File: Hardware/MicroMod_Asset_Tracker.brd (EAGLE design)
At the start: 76.2 x 76.2 mm, 338 parts, among them IC1 SN74AVC4T774PW, IC2 SN74AVC4T774PW, IC3 SN74AVC4T774PW, J11 microSD, J13 TP, J17 NANO_SIM, J18 SARA_USB, J19 NI, J2 JTAG, J4 MICROMOD-2222-C, J5 SPI, J6 DIAG, J7 QWIIC_RIGHT_ANGLE, J9 !RST!, Q1 310mA/60V/1.6Ω, Q10 20V/0.2A/8MHz/1.2Ω/1Vth, Q2 310mA/60V/1.6Ω, Q3 310mA/60V/1.6Ω, Q4 310mA/60V/1.6Ω, Q5 20V/0.2A/8MHz/1.2Ω/1Vth, Q6 20V/4.2A/52mΩ/1.4W, Q7 310mA/60V/1.6Ω, U1 SARA-R5, U13 9DoF IMU, U14 1.8V/100mA, U2 MCP73831, U3 3.3V, U5 AP7361C-33FGE, U7 PCA9306, U8 74HC1G04

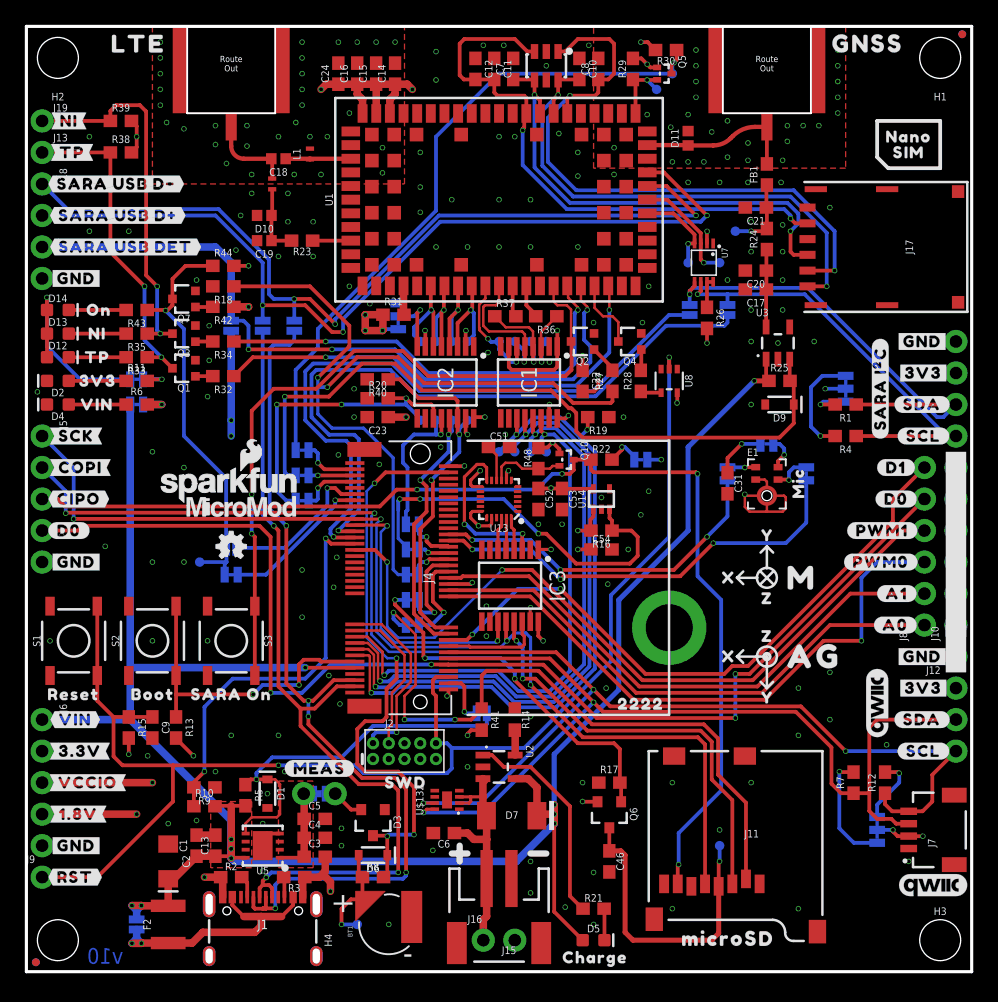
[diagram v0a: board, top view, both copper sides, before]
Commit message: Added the missing PROD_IDs
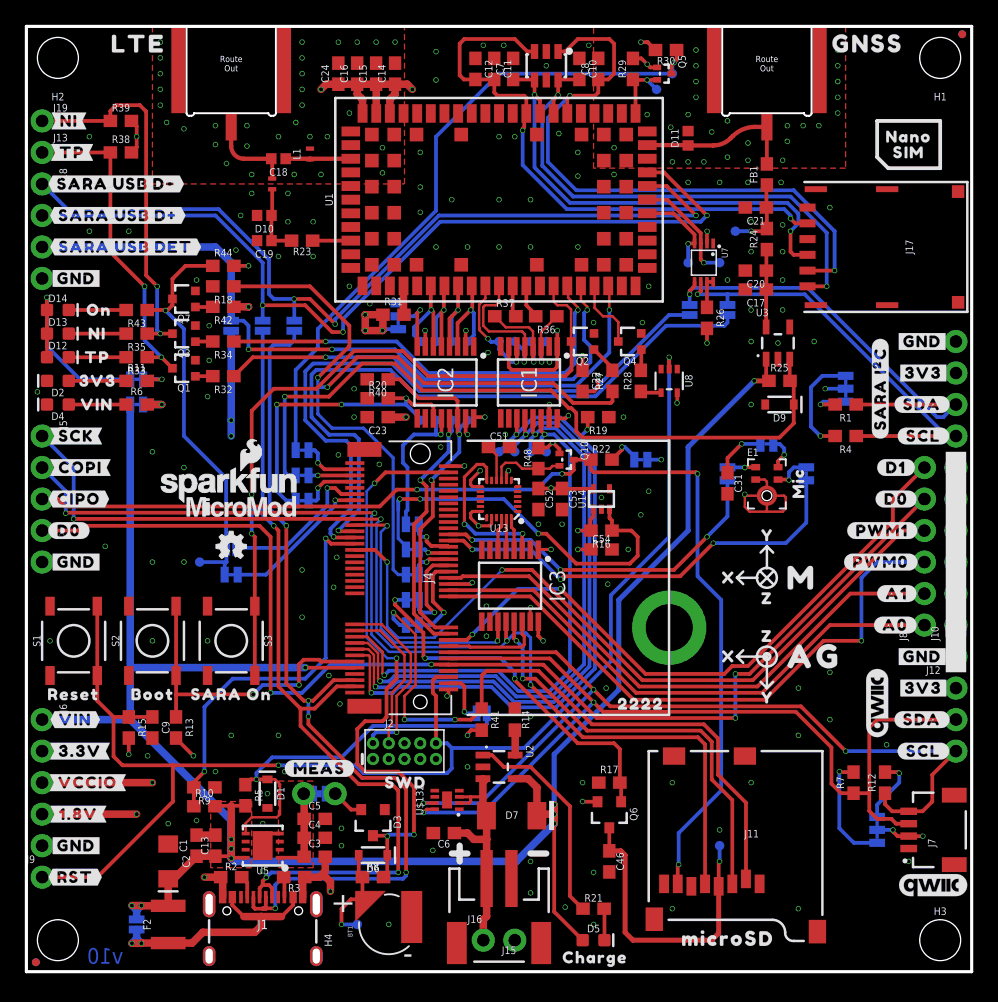
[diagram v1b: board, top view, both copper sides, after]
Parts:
- E3, E4: device New_Parts:SMA-EDGE-SMD -> SparkFun-RF:SMA-EDGE-SMD
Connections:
- net GND: now also U$132.1, U$132.4, U$132.6, U$132.9; no longer U$132.P$1, U$132.P$4, U$132.P$6, U$132.P$9
- net I2C_SCL: now also U$132.7; no longer U$132.P$7
- net I2C_SDA: now also U$132.8; no longer U$132.P$8
- net V_BATT: now also U$132.2, U$132.3; no longer U$132.P$2, U$132.P$3
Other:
- board text added: "HASL Finish"
- board text removed: "ENIG Finish"

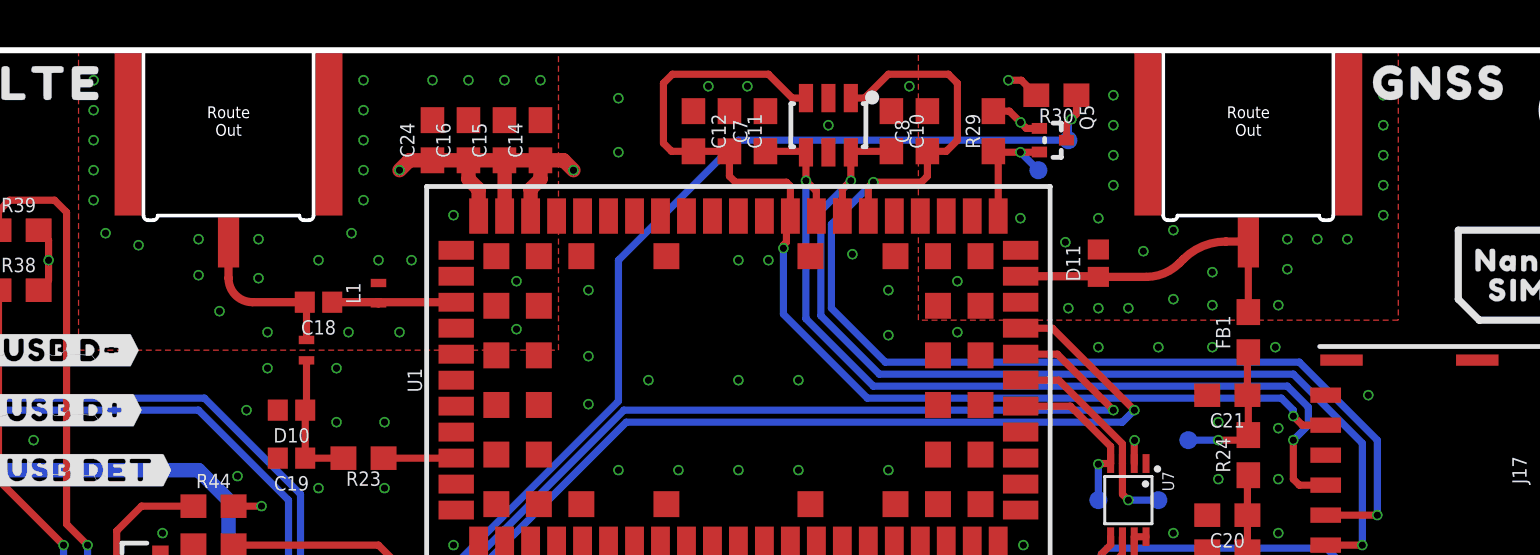
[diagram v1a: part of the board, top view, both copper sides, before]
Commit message: Updated to use the revised SMD SMA connector footprint
The footprint for the SMA now includes the toolpath for a 1mm end-mill
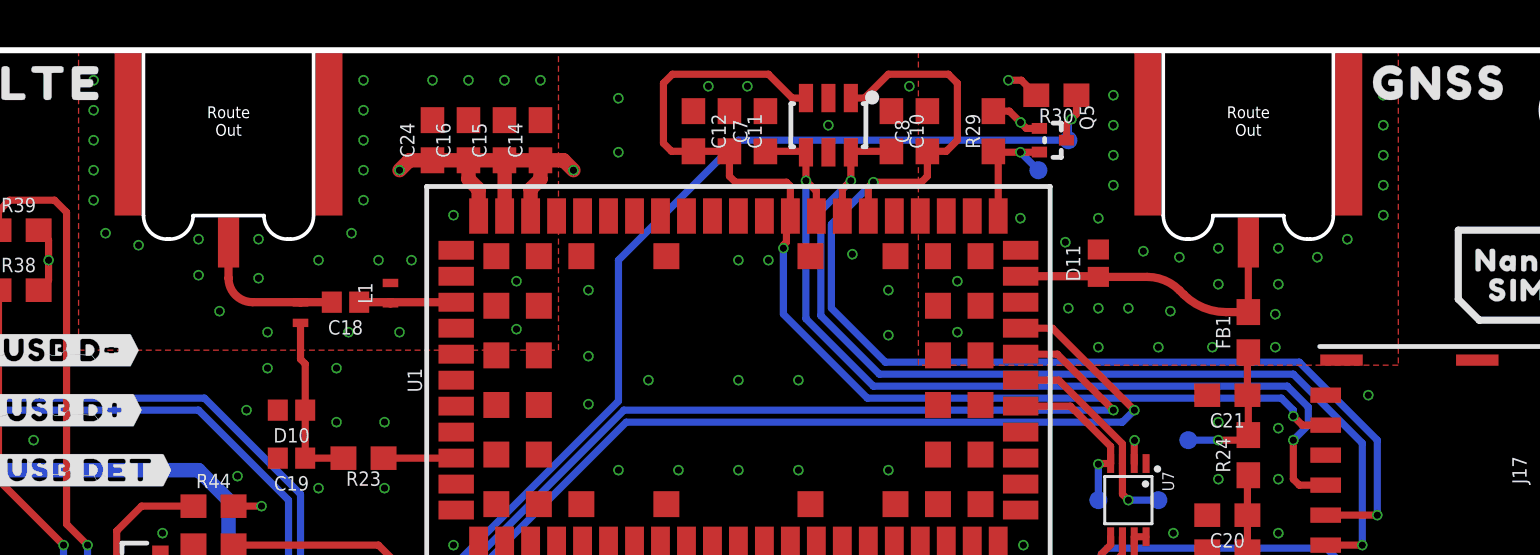
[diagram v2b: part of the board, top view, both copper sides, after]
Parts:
- moved L2 1.61 mm to (19.6, 65.1)
- moved C18 1.14 mm to (21.5, 65.5)
- moved L1 0.51 mm to (23.4, 65.9)
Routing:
- net N$16: track 5.78 -> 7.71 mm
- net SARA_ANT: track 5.29 -> 4.15 mm

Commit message: Updates for V11 of the PCB
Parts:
- removed R13: 100k, SparkFun-Resistors:0603
- added U$133: (no value), output:#VIN#3#0
- added VIN/3: JUMPER-SMT_2_NC_TRACE_SILK, SparkFun-Jumpers:SMT-JUMPER_2_NC_TRACE_SILK
- R33: value 470 -> 100
- moved U$28 1.05 mm to (50.9, 2.70)
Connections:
- new net N$18: R10.2, VIN/3.1
- net !BOOT!: no longer R13.1
- net 3.3V: no longer R13.2
- net VIN: now also VIN/3.2; no longer R10.2
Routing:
- net N$18: track 0.00 -> 4.38 mm, vias 0 -> 1
- net !BOOT!: track 25.5 -> 23.5 mm
- net 3.3V: track 69.1 -> 67.1 mm, vias 24 -> 23
- net GND: vias 191 -> 192
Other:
- board text added: "v11"
- board text removed: "v10"
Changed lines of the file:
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@@
 <?xml version="1.0" encoding="utf-8"?>
 <!DOCTYPE eagle SYSTEM "eagle.dtd">
-<eagle version="9.6.0">
+<eagle version="9.6.2">
 <drawing>
 <settings>
@@
 <wire x1="76.2" y1="0" x2="0" y2="0" width="0.254" layer="20"/>
 <rectangle x1="74.1045" y1="26.9875" x2="75.7555" y2="41.91" layer="21"/>
-<text x="6.35" y="1.27" size="1.27" layer="16" font="vector" ratio="20" rot="MR0" align="center">v10</text>
+<text x="6.35" y="1.27" size="1.27" layer="16" font="vector" ratio="20" rot="MR0" align="center">v11</text>
 <wire x1="35.56" y1="42.799" x2="51.805" y2="42.799" width="0.2032" layer="21"/>
 <wire x1="51.805" y1="42.799" x2="51.805" y2="20.701" width="0.2032" layer="21"/>
@@
 <element name="U$4" library="output" package="#3V3#0" value="" x="8.001" y="47.752" smashed="yes" rot="MR0"/>
 <element name="U$20" library="output" package="#VIN#1" value="" x="8.001" y="45.72" smashed="yes" rot="MR0"/>
-<element name="U$28" library="output" package="MICROSD0" value="" x="51.943" y="2.667" smashed="yes"/>
+<element name="U$28" library="output" package="MICROSD0" value="" x="50.89525" y="2.69875" smashed="yes"/>
 <element name="LOGO5" library="SparkFun-Aesthetics" package="ORDERING_INSTRUCTIONS" value="SPECIAL_INSTRUCTIONS-ORDERING" x="80.01" y="50.8" smashed="yes"/>
 <element name="J7" library="SparkFun-Connectors" package="JST04_1MM_RA" value="QWIIC_RIGHT_ANGLE" x="71.12" y="11.43" smashed="yes" rot="R90">
@@
 <attribute name="VALUE" x="9.398" y="19.685" size="0.6096" layer="27" font="vector" ratio="20" rot="R270" align="top-center"/>
 </element>
-<element name="R13" library="SparkFun-Resistors" package="0603" value="100k" x="12.065" y="19.685" smashed="yes" rot="R270">
-<attribute name="NAME" x="12.827" y="19.685" size="0.6096" layer="25" font="vector" ratio="20" rot="R270" align="bottom-center"/>
-<attribute name="PROD_ID" value="RES-07828" x="12.065" y="19.685" size="1.778" layer="27" ratio="15" rot="R270" display="off"/>
-<attribute name="VALUE" x="11.303" y="19.685" size="0.6096" layer="27" font="vector" ratio="20" rot="R270" align="top-center"/>
-</element>
 <element name="U1" library="SARA_R5" package="SARA-LGA" value="SARA-R5" x="38.1" y="62.23" smashed="yes">
 <attribute name="NAME" x="24.7" y="62.23" size="0.6096" layer="25" font="vector" ratio="20" rot="R90" align="bottom-center"/>
@@
 <attribute name="VALUE" x="15.875" y="48.768" size="0.6096" layer="27" font="vector" ratio="20" rot="R180" align="top-center"/>
 </element>
-<element name="R33" library="SparkFun-Resistors" package="0603" value="470" x="8.89" y="49.53" smashed="yes" rot="R180">
+<element name="R33" library="SparkFun-Resistors" package="0603" value="100" x="8.89" y="49.53" smashed="yes" rot="R180">
 <attribute name="NAME" x="8.89" y="48.768" size="0.6096" layer="25" font="vector" ratio="20" rot="R180" align="bottom-center"/>
-<attribute name="PROD_ID" value="RES-07869" x="8.89" y="49.53" size="1.778" layer="27" ratio="15" rot="R180" display="off"/>
-<attribute name="VALUE" value="470" x="8.89" y="50.292" size="0.6096" layer="27" font="vector" ratio="20" rot="R180" align="top-center"/>
+<attribute name="PROD_ID" value="RES-07863" x="8.89" y="49.53" size="1.778" layer="27" ratio="15" rot="R180" display="off"/>
+<attribute name="VALUE" value="100" x="8.89" y="50.292" size="0.6096" layer="27" font="vector" ratio="20" rot="R180" align="top-center"/>
 </element>
 <element name="D12" library="SparkFun-LED" package="LED-0603" value="GREEN" x="2.54" y="49.53" smashed="yes">
@@
 <attribute name="VALUE" x="36.449" y="13.843" size="0.6096" layer="27" font="vector" ratio="20" rot="R90" align="bottom-center"/>
 </element>
+<element name="VIN/3" library="SparkFun-Jumpers" package="SMT-JUMPER_2_NC_TRACE_SILK" package3d_urn="urn:adsk.eagle:package:39281/1" value="JUMPER-SMT_2_NC_TRACE_SILK" x="16.47825" y="14.63675" smashed="yes" rot="MR270">
+<attribute name="NAME" x="15.33525" y="14.63675" size="0.6096" layer="26" font="vector" ratio="20" rot="MR270" align="bottom-center"/>
+</element>
+<element name="U$133" library="output" package="#VIN#3#0" value="" x="14.478" y="14.70025" smashed="yes" rot="MR270"/>
 </elements>
 <signals>
@@
 <contactref element="U$132" pad="6"/>
 <via x="46.736" y="22.86" extent="1-16" drill="0.3"/>
+<via x="17.653" y="16.0655" extent="1-16" drill="0.3"/>
 </signal>
 <signal name="3.3V">
@@
 <contactref element="J12" pad="2"/>
 <contactref element="R15" pad="2"/>
-<contactref element="R13" pad="2"/>
 <contactref element="C54" pad="1"/>
 <contactref element="U14" pad="1"/>
@@
 <wire x1="50.077" y1="74.93" x2="49.53" y2="74.93" width="0.3048" layer="1"/>
 <via x="8.255" y="17.526" extent="1-16" drill="0.3"/>
-<via x="13.462" y="17.399" extent="1-16" drill="0.3"/>
 <wire x1="8.255" y1="18.835" x2="8.255" y2="17.526" width="0.3048" layer="1"/>
-<wire x1="12.065" y1="18.835" x2="12.065" y2="18.796" width="0.3048" layer="1"/>
-<wire x1="12.065" y1="18.796" x2="13.462" y2="17.399" width="0.3048" layer="1"/>
 <via x="35.306" y="40.767" extent="1-16" drill="0.3"/>
 <wire x1="34.025" y1="40.75" x2="35.289" y2="40.75" width="0.3048" layer="1"/>
@@
 <contactref element="BYP" pad="2"/>
 <contactref element="F2" pad="2"/>
-<contactref element="R10" pad="2"/>
 <contactref element="C1" pad="1"/>
 <contactref element="R5" pad="2"/>
@@
 <wire x1="13.716" y1="9.31" x2="15.24" y2="9.31" width="0.6096" layer="1"/>
 <wire x1="15.365" y1="9.185" x2="15.24" y2="9.31" width="0.3048" layer="1"/>
-<wire x1="15.201" y1="13.335" x2="15.24" y2="13.374" width="0.3048" layer="1"/>
-<wire x1="15.24" y1="13.374" x2="16.51" y2="13.374" width="0.3048" layer="1"/>
 <wire x1="16.51" y1="13.374" x2="17.653" y2="13.374" width="0.3048" layer="1"/>
 <via x="16.51" y="9.144" extent="1-16" drill="0.3"/>
@@
 <wire x1="16.51" y1="10.668" x2="16.51" y2="12.192" width="0.6096" layer="16"/>
 <wire x1="8.382" y1="20.32" x2="1.27" y2="20.32" width="0.6096" layer="16"/>
-<wire x1="16.51" y1="12.192" x2="8.382" y2="20.32" width="0.6096" layer="16"/>
+<wire x1="16.51" y1="12.192" x2="15.922625" y2="12.779375" width="0.6096" layer="16"/>
+<wire x1="15.922625" y1="12.779375" x2="8.382" y2="20.32" width="0.6096" layer="16"/>
 <wire x1="8.3693" y1="45.72" x2="8.3693" y2="24.511" width="0.6096" layer="16"/>
 <wire x1="8.3693" y1="24.511" x2="8.3693" y2="20.3327" width="0.6096" layer="16"/>
@@
 <wire x1="41.154" y1="14.853" x2="41.154" y2="12.573" width="0.6096" layer="1"/>
 <wire x1="40.447" y1="15.56" x2="41.154" y2="14.853" width="0.6096" layer="1"/>
+<contactref element="VIN/3" pad="2"/>
+<wire x1="16.47825" y1="14.11605" x2="16.47825" y2="13.335" width="0.3048" layer="16"/>
+<wire x1="16.47825" y1="13.335" x2="15.922625" y2="12.779375" width="0.3048" layer="16"/>
 </signal>
 <signal name="VIN/3">
@@
 <contactref element="S2" pad="4"/>
 <contactref element="J4" pad="11"/>
-<contactref element="R13" pad="1"/>
-<wire x1="12.065" y1="20.535" x2="12.065" y2="22.352" width="0.3048" layer="1"/>
-<wire x1="12.065" y1="22.352" x2="12.065" y2="23.876" width="0.3048" layer="1"/>
+<wire x1="18.288" y1="22.352" x2="12.41425" y2="22.352" width="0.3048" layer="1"/>
+<wire x1="12.41425" y1="22.352" x2="12.065" y2="22.70125" width="0.3048" layer="1"/>
+<wire x1="12.065" y1="22.70125" x2="12.065" y2="23.876" width="0.3048" layer="1"/>
 <wire x1="12.065" y1="23.876" x2="12.065" y2="29.464" width="0.3048" layer="1"/>
-<wire x1="18.288" y1="22.352" x2="12.065" y2="22.352" width="0.3048" layer="1"/>
 <wire x1="26.475" y1="25" x2="23.74986875" y2="25" width="0.3048" layer="1"/>
 <wire x1="23.74986875" y1="25" x2="23.60386875" y2="25.146" width="0.3048" layer="1"/>
@@
 <wire x1="31.507" y1="53.097" x2="31.507" y2="50.398" width="0.3048" layer="1"/>
 </signal>
+<signal name="N$18">
+<contactref element="VIN/3" pad="1"/>
+<contactref element="R10" pad="2"/>
+<wire x1="16.47825" y1="15.15745" x2="16.47825" y2="16.09725" width="0.3048" layer="16"/>
+<via x="16.47825" y="16.09725" extent="1-16" drill="0.3"/>
+<wire x1="16.47825" y1="16.09725" x2="16.47825" y2="14.35825" width="0.3048" layer="1"/>
+<wire x1="16.47825" y1="14.35825" x2="15.455" y2="13.335" width="0.3048" layer="1"/>
+<wire x1="15.455" y1="13.335" x2="15.201" y2="13.335" width="0.3048" layer="1"/>
+</signal>
 </signals>

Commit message: v11
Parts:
- removed D9: 3.3V, SparkFun-DiscreteSemi:SOD-323
- removed JP19: JUMPER-SMT_2_NC_TRACE_SILK, SparkFun-Jumpers:SMT-JUMPER_2_NC_TRACE_SILK
- removed JP21: JUMPER-SMT_2_NO_SILK, SparkFun-Jumpers:SMT-JUMPER_2_NO_SILK
- removed U$118, U$119: (no value), output:#SARA_#ON##0
- removed U$120: (no value), output:#G10#0
- removed U$121: (no value), output:#G9#0
- added JP9: JUMPER-SMT_2_NC_TRACE_SILK, SparkFun-Jumpers:SMT-JUMPER_2_NC_TRACE_SILK
- added Q8, Q9: 310mA/60V/1.6Ω, SparkFun-DiscreteSemi:SOT323
- added R13: 1k, SparkFun-Resistors:0603
- added R45: 100k, SparkFun-Resistors:0603
- added U$134: (no value), output:#ICM_INT#0
- JP13, JP14, JP15, JP16, JP17: value JUMPER-SMT_2_NC_TRACE_SILK -> JUMPER-SMT_2_NO_SILK; device SparkFun-Jumpers:SMT-JUMPER_2_NC_TRACE_SILK -> SparkFun-Jumpers:SMT-JUMPER_2_NO_SILK
- R35: value 1k -> 470
- U$110: device output:#ANT_PWR#0 -> output:#SARA_#ON##0
- moved TP13 7.73 mm to (12.7, 40.6)
- moved R25 3.56 mm to (58.0, 45.3), turned to 270 degrees
- moved U$110 0.25 mm to (17.4, 40.0)
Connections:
- removed net G10: J4.63, JP19.1
- removed net G9: J4.65, JP21.1
- new net ANT_REG_EN: Q9.3, R45.2, U3.3
- new net N$19: J4.16, JP9.2
- new net N$40: Q8.1, R13.2
- new net N$42: Q8.3, Q9.1, R25.2
- net 3.3V: now also R25.1, R45.1
- net ANT_GNSS_PWR_EN: now also R13.1, U1.23; no longer D9.C, JP16.2, R25.2, U3.3
- net GND: now also Q8.2, Q9.2; no longer D9.A
- net ICM_INT: now also JP9.1; no longer J4.16
- net SARA_!ON!: now also JP16.2; no longer JP19.2, JP21.2
- net VIN: no longer R25.1
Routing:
- net ANT_GNSS_PWR_EN: track 58.3 -> 11.9 mm, vias 1 -> 0
- net G9: track 12.6 -> 0.00 mm, vias 1 -> 0
- net G10: track 12.2 -> 0.00 mm, vias 1 -> 0
- net N$19: track 0.00 -> 7.01 mm, vias 0 -> 1
- net ICM_INT: track 8.14 -> 2.20 mm, vias 0 -> 1
- net ANT_REG_EN: track 0.00 -> 4.02 mm
- net N$42: track 0.00 -> 3.80 mm
- net 3.3V: track 67.1 -> 70.4 mm, vias 23 -> 24
- net GND: track 30.6 -> 33.4 mm, vias 192 -> 195
- net N$40: track 0.00 -> 1.69 mm
- net D1: track 50.8 -> 51.8 mm
- net SARA_!ON!: track 33.6 -> 33.1 mm, vias 1 -> 3
